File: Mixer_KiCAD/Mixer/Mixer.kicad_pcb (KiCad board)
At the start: 4 copper layers, 78 x 52.7 mm, 63 parts, among them IC1 HMC220BMS8GETR, IC2 LMX2572RHAT, IC3 HMC220BMS8GETR, IC4 TPS74601PQWDRBRQ1, IC5 MCP2210-I_MQ, J1 CONSMA020.062-G, J2 CONSMA020.062-G, J3 CONSMA020.062-G, J4 CONSMA020.062-G, J5 USB4940-00-A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

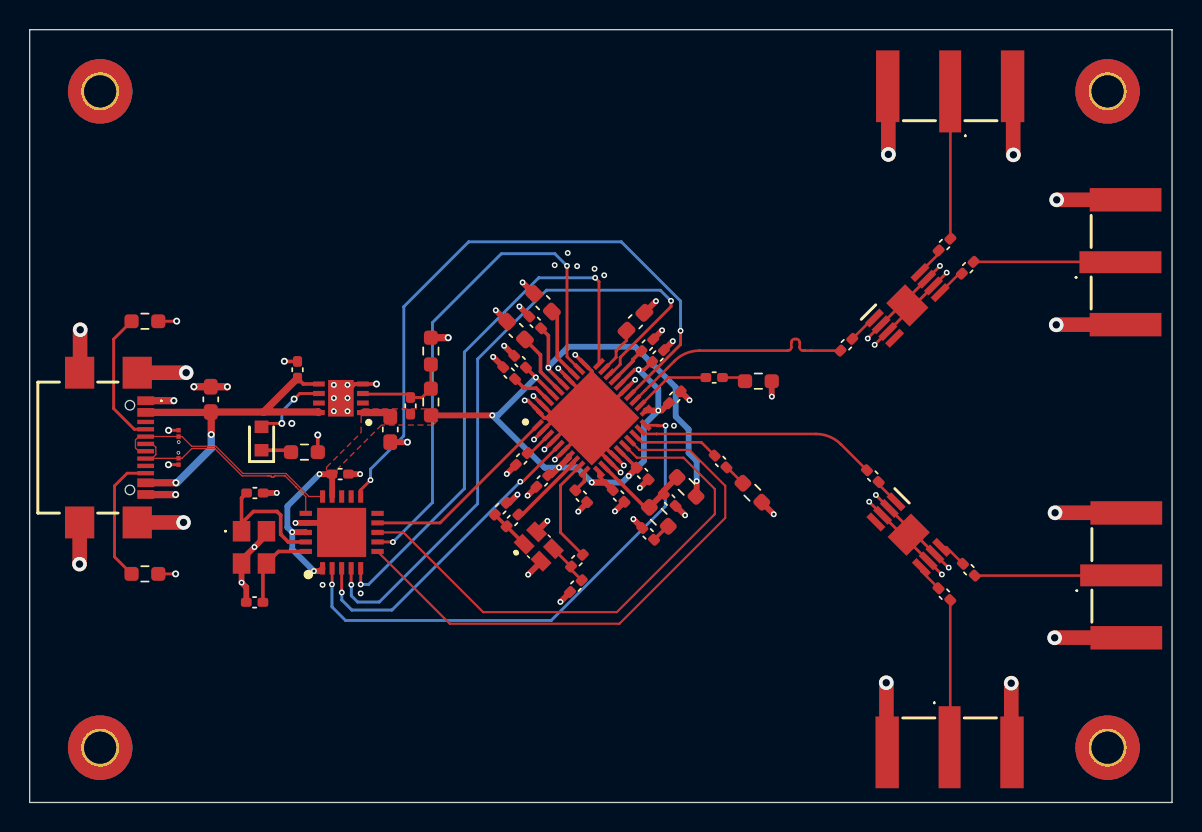
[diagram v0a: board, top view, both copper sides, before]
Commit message: added stitching vias to pcb
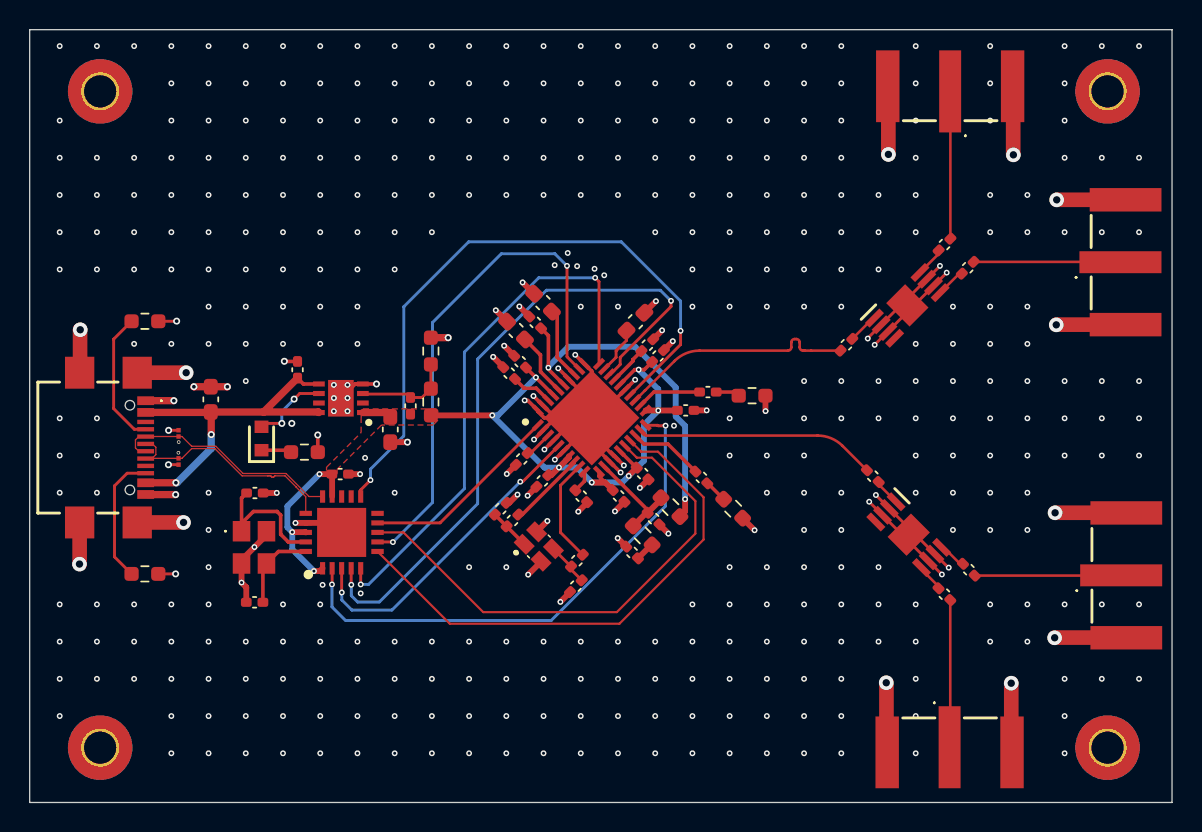
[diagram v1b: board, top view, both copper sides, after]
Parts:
- moved R3 1.77 mm to (98.2, 149.3)
- moved C7 1.70 mm to (100.3, 147.3)
- moved R2 1.70 mm to (102.5, 149.4)
- moved R4 1.68 mm to (96.3, 151.2)
- moved C17 1.68 mm to (95.6, 152.4)
- moved C14 1.68 mm to (97.1, 150.1)
- moved C1 1.16 mm to (99.3, 142.7), turned to 0 degrees
- moved C5 1.08 mm to (100.8, 141.5)
- moved R1 1.08 mm to (103.8, 141.7)
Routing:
- net /SDI: track 38.7 -> 36.2 mm
- net /SCK: track 37.1 -> 34.8 mm
- net Net-(IC2-VTUNE): track 22.9 -> 24.1 mm
- net Net-(IC2-RFOUTBM): track 5.99 -> 5.13 mm
- net Net-(IC2-RFOUTAM): track 5.25 -> 4.41 mm
- net GND: vias 85 -> 451
